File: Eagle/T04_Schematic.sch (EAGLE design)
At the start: 19 parts

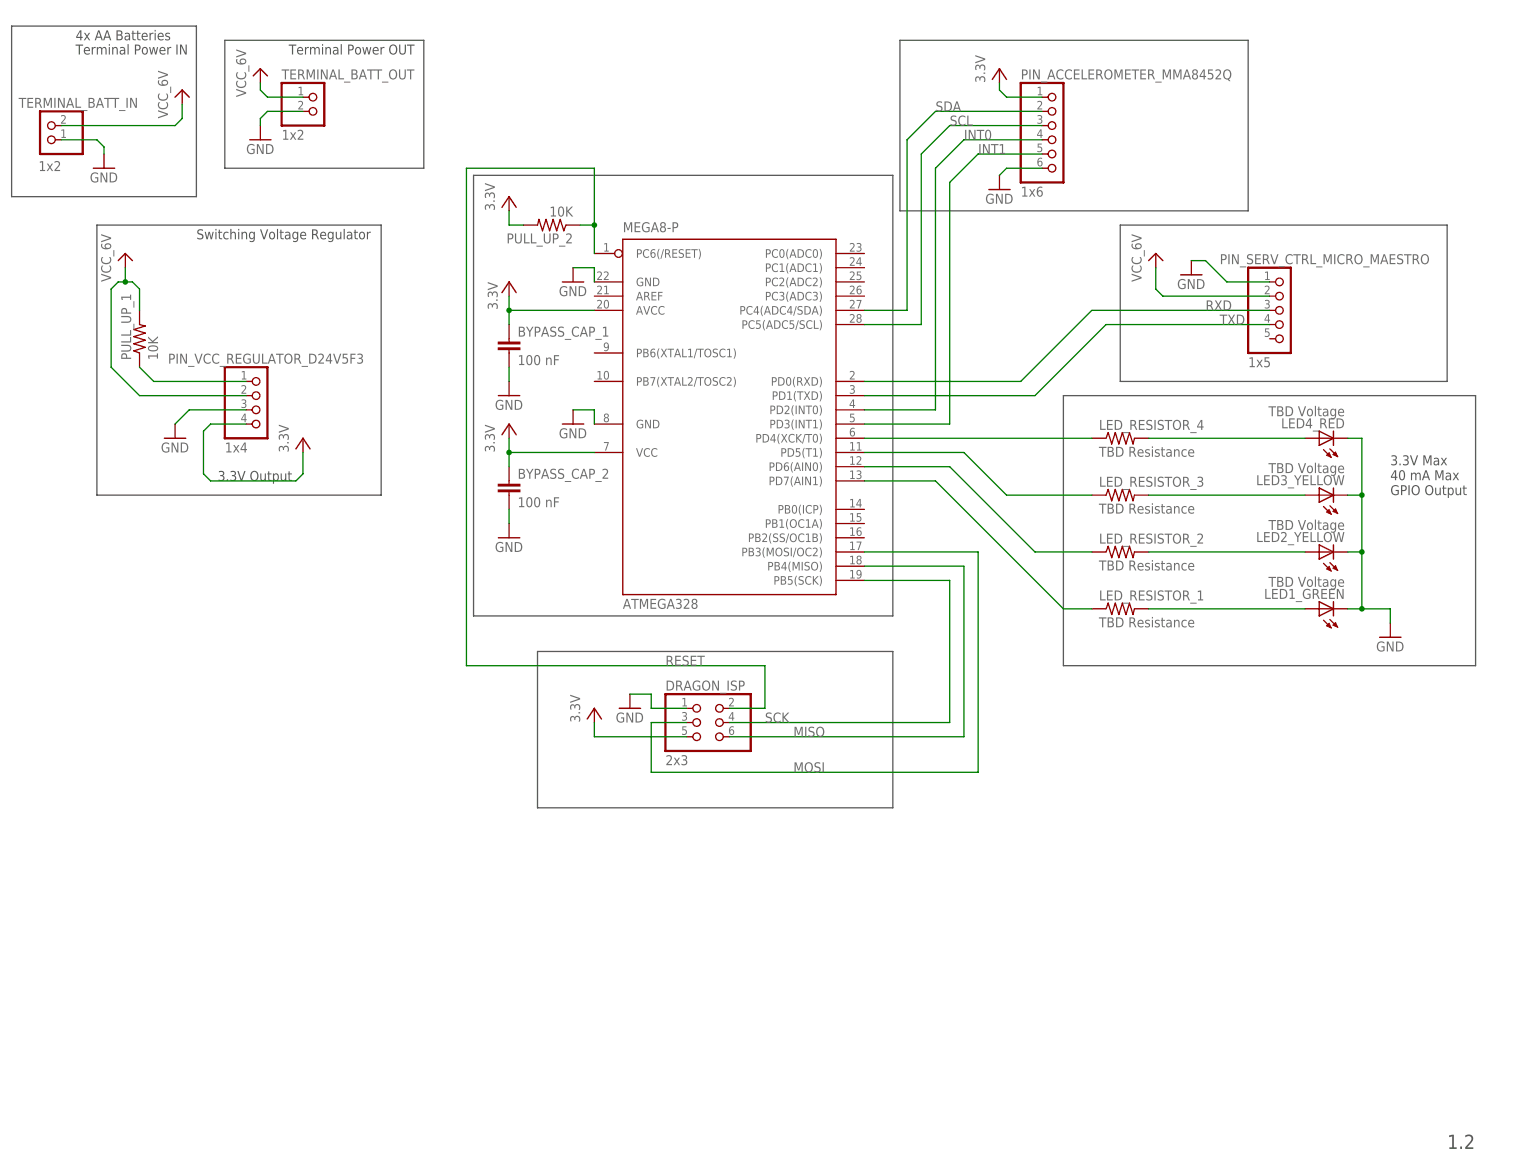
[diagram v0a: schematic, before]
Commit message: Schematic Updates
Updated with better supply layout and more organization.
Also changed filename to have team name.
Still Need: Oscillator, LEDs, UART review
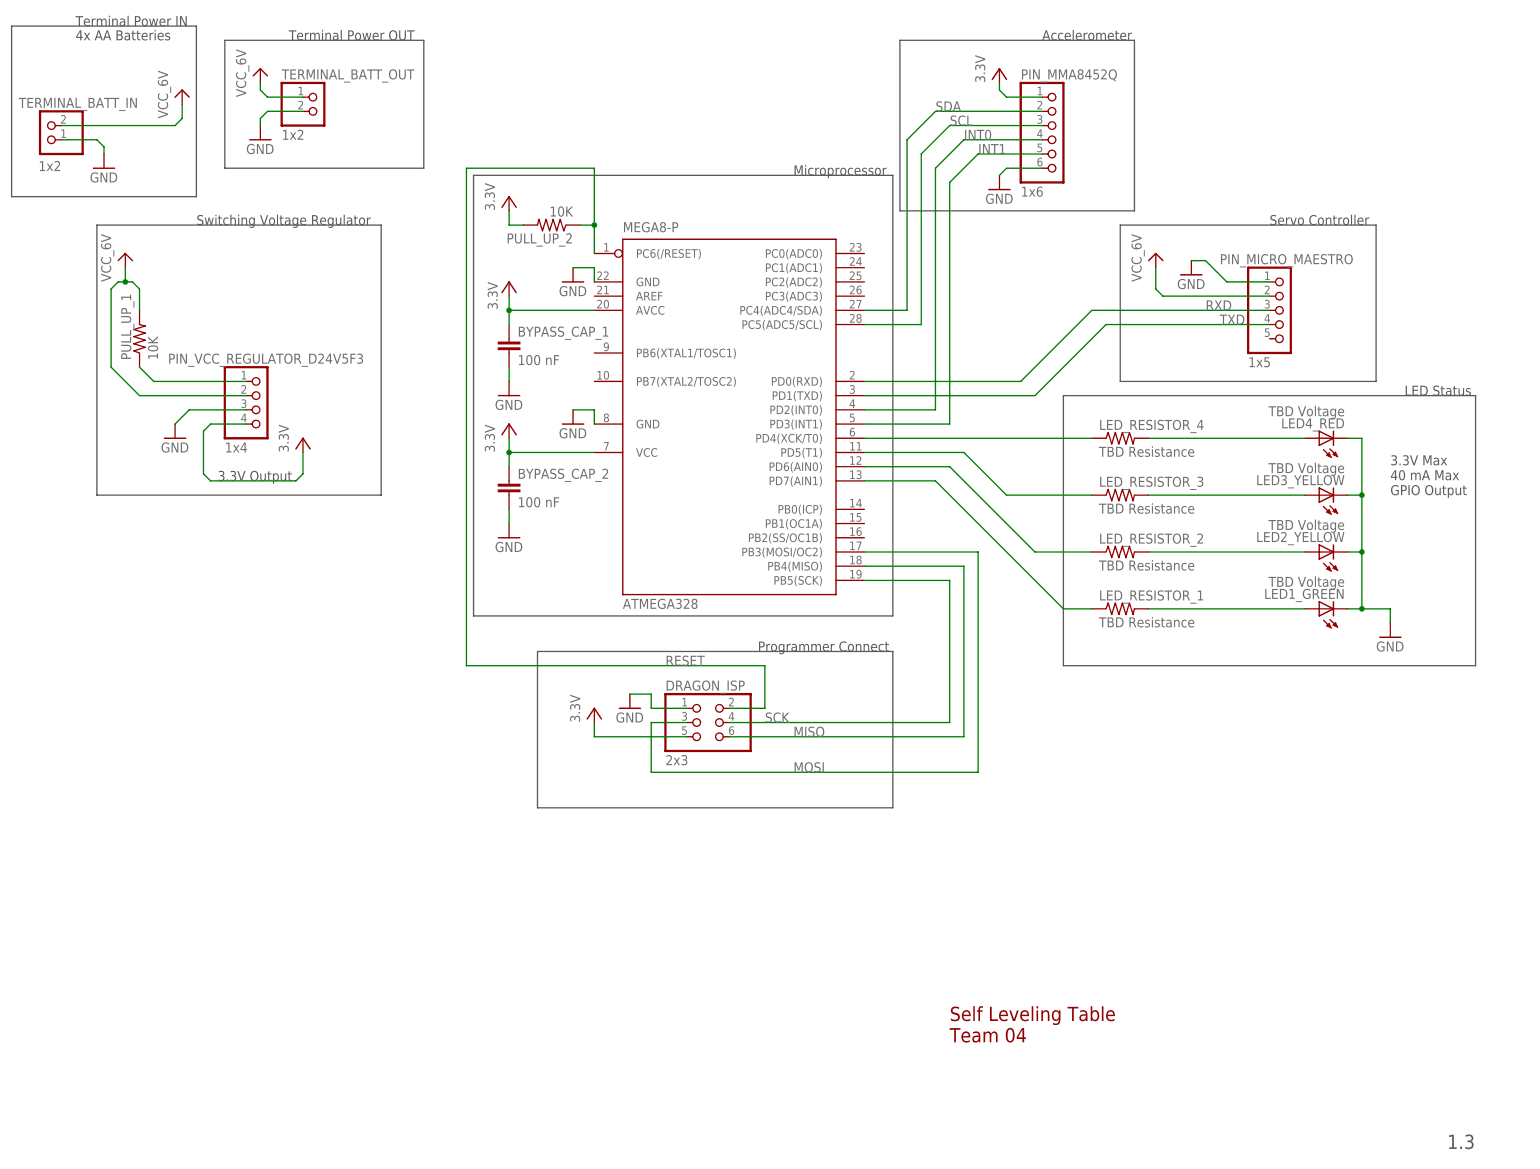
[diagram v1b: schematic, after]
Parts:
- renumbered PIN_ACCELEROMETER_MMA8452Q to PIN_MMA8452Q, PIN_SERV_CTRL_MICRO_MAESTRO to PIN_MICRO_MAESTRO
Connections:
- net VCC_3.3V renamed VCC
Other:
- note added: "1.3"
- note added: "Accelerometer"
- note added: "LED Status"
- note added: "Microprocessor"
- note added: "Programmer Connect"
- note added: "Self Leveling Table Team 04"
- note added: "Servo Controller"
- note removed: "1.2"
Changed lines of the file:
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@@
 <part name="FRAME1" library="frames" deviceset="FRAME_A_L" device=""/>
 <part name="ATMEGA328" library="atmel" deviceset="MEGA8-P" device=""/>
-<part name="PIN_ACCELEROMETER_MMA8452Q" library="pinhead" deviceset="PINHD-1X6" device="" value="1x6"/>
-<part name="PIN_SERV_CTRL_MICRO_MAESTRO" library="pinhead" deviceset="PINHD-1X5" device="" value="1x5"/>
+<part name="PIN_MMA8452Q" library="pinhead" deviceset="PINHD-1X6" device="" value="1x6"/>
+<part name="PIN_MICRO_MAESTRO" library="pinhead" deviceset="PINHD-1X5" device="" value="1x5"/>
 <part name="PIN_VCC_REGULATOR_D24V5F3" library="pinhead" deviceset="PINHD-1X4" device="" value="1x4"/>
 <part name="TERMINAL_BATT_IN" library="pinhead" deviceset="PINHD-1X2" device="" value="1x2"/>
@@
 <plain>
 <text x="6.35" y="154.94" size="1.778" layer="97">4x AA Batteries</text>
-<text x="251.46" y="-43.18" size="2.54" layer="97">1.2</text>
+<text x="251.46" y="-43.18" size="2.54" layer="97">1.3</text>
 <text x="241.3" y="73.66" size="1.778" layer="97">3.3V Max
 40 mA Max
@@
 <wire x1="256.54" y1="43.18" x2="182.88" y2="43.18" width="0.1524" layer="97"/>
 <wire x1="182.88" y1="43.18" x2="182.88" y2="91.44" width="0.1524" layer="97"/>
-<wire x1="153.67" y1="154.94" x2="215.9" y2="154.94" width="0.1524" layer="97"/>
-<wire x1="215.9" y1="154.94" x2="215.9" y2="124.46" width="0.1524" layer="97"/>
-<wire x1="215.9" y1="124.46" x2="153.67" y2="124.46" width="0.1524" layer="97"/>
+<wire x1="153.67" y1="154.94" x2="195.58" y2="154.94" width="0.1524" layer="97"/>
+<wire x1="195.58" y1="154.94" x2="195.58" y2="124.46" width="0.1524" layer="97"/>
+<wire x1="195.58" y1="124.46" x2="153.67" y2="124.46" width="0.1524" layer="97"/>
 <wire x1="153.67" y1="124.46" x2="153.67" y2="154.94" width="0.1524" layer="97"/>
-<wire x1="193.04" y1="121.92" x2="251.46" y2="121.92" width="0.1524" layer="97"/>
-<wire x1="251.46" y1="121.92" x2="251.46" y2="93.98" width="0.1524" layer="97"/>
-<wire x1="251.46" y1="93.98" x2="193.04" y2="93.98" width="0.1524" layer="97"/>
+<wire x1="193.04" y1="121.92" x2="238.76" y2="121.92" width="0.1524" layer="97"/>
+<wire x1="238.76" y1="121.92" x2="238.76" y2="93.98" width="0.1524" layer="97"/>
+<wire x1="238.76" y1="93.98" x2="193.04" y2="93.98" width="0.1524" layer="97"/>
 <wire x1="193.04" y1="93.98" x2="193.04" y2="121.92" width="0.1524" layer="97"/>
 <wire x1="88.9" y1="45.72" x2="152.4" y2="45.72" width="0.1524" layer="97"/>
@@
 <wire x1="152.4" y1="52.07" x2="77.47" y2="52.07" width="0.1524" layer="97"/>
 <wire x1="77.47" y1="52.07" x2="77.47" y2="130.81" width="0.1524" layer="97"/>
-<text x="6.35" y="152.4" size="1.778" layer="97">Terminal Power IN</text>
-<text x="44.45" y="152.4" size="1.778" layer="97">Terminal Power OUT</text>
-<text x="27.94" y="119.38" size="1.778" layer="97">Switching Voltage Regulator</text>
+<text x="6.35" y="157.48" size="1.778" layer="97">Terminal Power IN</text>
+<text x="44.45" y="154.94" size="1.778" layer="97">Terminal Power OUT</text>
+<text x="27.94" y="121.92" size="1.778" layer="97">Switching Voltage Regulator</text>
+<text x="162.56" y="-24.13" size="2.54" layer="94">Self Leveling Table
+Team 04</text>
+<text x="179.07" y="154.94" size="1.778" layer="97">Accelerometer</text>
+<text x="219.71" y="121.92" size="1.778" layer="97">Servo Controller</text>
+<text x="243.84" y="91.44" size="1.778" layer="97">LED Status</text>
+<text x="128.27" y="45.72" size="1.778" layer="97">Programmer Connect</text>
+<text x="134.62" y="130.81" size="1.778" layer="97">Microprocessor</text>
 </plain>
 <instances>
@@
 <instance part="FRAME1" gate="G$2" x="158.75" y="-50.8"/>
 <instance part="ATMEGA328" gate="G$1" x="121.92" y="88.9"/>
-<instance part="PIN_ACCELEROMETER_MMA8452Q" gate="A" x="181.61" y="137.16"/>
-<instance part="PIN_SERV_CTRL_MICRO_MAESTRO" gate="A" x="222.25" y="106.68" smashed="yes">
+<instance part="PIN_MMA8452Q" gate="A" x="181.61" y="137.16"/>
+<instance part="PIN_MICRO_MAESTRO" gate="A" x="222.25" y="106.68" smashed="yes">
 <attribute name="NAME" x="210.82" y="114.935" size="1.778" layer="95"/>
 <attribute name="VALUE" x="215.9" y="96.52" size="1.778" layer="96"/>
@@
 </segment>
 <segment>
-<pinref part="PIN_ACCELEROMETER_MMA8452Q" gate="A" pin="6"/>
+<pinref part="PIN_MMA8452Q" gate="A" pin="6"/>
 <pinref part="GND3" gate="1" pin="GND"/>
 <wire x1="171.45" y1="130.81" x2="172.72" y2="132.08" width="0.1524" layer="91"/>
@@
 <pinref part="GND4" gate="1" pin="GND"/>
 <wire x1="205.74" y1="115.57" x2="208.28" y2="115.57" width="0.1524" layer="91"/>
-<pinref part="PIN_SERV_CTRL_MICRO_MAESTRO" gate="A" pin="1"/>
+<pinref part="PIN_MICRO_MAESTRO" gate="A" pin="1"/>
 <wire x1="208.28" y1="115.57" x2="212.09" y2="111.76" width="0.1524" layer="91"/>
 <wire x1="212.09" y1="111.76" x2="219.71" y2="111.76" width="0.1524" layer="91"/>
@@
 <net name="SDA" class="0">
 <segment>
-<pinref part="PIN_ACCELEROMETER_MMA8452Q" gate="A" pin="2"/>
+<pinref part="PIN_MMA8452Q" gate="A" pin="2"/>
 <wire x1="179.07" y1="142.24" x2="160.02" y2="142.24" width="0.1524" layer="91"/>
 <label x="160.02" y="142.24" size="1.778" layer="95"/>
@@
 <net name="SCL" class="0">
 <segment>
-<pinref part="PIN_ACCELEROMETER_MMA8452Q" gate="A" pin="3"/>
+<pinref part="PIN_MMA8452Q" gate="A" pin="3"/>
 <wire x1="179.07" y1="139.7" x2="162.56" y2="139.7" width="0.1524" layer="91"/>
 <label x="162.56" y="139.7" size="1.778" layer="95"/>
@@
 <net name="INT0" class="0">
 <segment>
-<pinref part="PIN_ACCELEROMETER_MMA8452Q" gate="A" pin="4"/>
+<pinref part="PIN_MMA8452Q" gate="A" pin="4"/>
 <wire x1="179.07" y1="137.16" x2="165.1" y2="137.16" width="0.1524" layer="91"/>
 <label x="165.1" y="137.16" size="1.778" layer="95"/>
@@
 <pinref part="ATMEGA328" gate="G$1" pin="PD3(INT1)"/>
 <wire x1="162.56" y1="86.36" x2="147.32" y2="86.36" width="0.1524" layer="91"/>
-<pinref part="PIN_ACCELEROMETER_MMA8452Q" gate="A" pin="5"/>
+<pinref part="PIN_MMA8452Q" gate="A" pin="5"/>
 <wire x1="179.07" y1="134.62" x2="167.64" y2="134.62" width="0.1524" layer="91"/>
 <label x="167.64" y="134.62" size="1.778" layer="95"/>
@@
 </segment>
 </net>
-<net name="VCC_3.3V" class="0">
+<net name="VCC" class="0">
 <segment>
 <pinref part="P+1" gate="VCC" pin="VCC"/>
@@
 </segment>
 <segment>
-<pinref part="PIN_ACCELEROMETER_MMA8452Q" gate="A" pin="1"/>
+<pinref part="PIN_MMA8452Q" gate="A" pin="1"/>
 <wire x1="172.72" y1="144.78" x2="179.07" y2="144.78" width="0.1524" layer="91"/>
 <pinref part="P+5" gate="VCC" pin="VCC"/>
@@
 <pinref part="ATMEGA328" gate="G$1" pin="PD0(RXD)"/>
 <wire x1="147.32" y1="93.98" x2="175.26" y2="93.98" width="0.1524" layer="91"/>
-<pinref part="PIN_SERV_CTRL_MICRO_MAESTRO" gate="A" pin="3"/>
+<pinref part="PIN_MICRO_MAESTRO" gate="A" pin="3"/>
 <wire x1="187.96" y1="106.68" x2="219.71" y2="106.68" width="0.1524" layer="91"/>
 <label x="208.28" y="106.68" size="1.778" layer="95"/>
@@
 <pinref part="ATMEGA328" gate="G$1" pin="PD1(TXD)"/>
 <wire x1="147.32" y1="91.44" x2="177.8" y2="91.44" width="0.1524" layer="91"/>
-<pinref part="PIN_SERV_CTRL_MICRO_MAESTRO" gate="A" pin="4"/>
+<pinref part="PIN_MICRO_MAESTRO" gate="A" pin="4"/>
 <wire x1="190.5" y1="104.14" x2="219.71" y2="104.14" width="0.1524" layer="91"/>
 <label x="210.82" y="104.14" size="1.778" layer="95"/>
@@
 </segment>
 <segment>
-<pinref part="PIN_SERV_CTRL_MICRO_MAESTRO" gate="A" pin="2"/>
+<pinref part="PIN_MICRO_MAESTRO" gate="A" pin="2"/>
 <wire x1="219.71" y1="109.22" x2="200.66" y2="109.22" width="0.1524" layer="91"/>
 <wire x1="200.66" y1="109.22" x2="199.39" y2="110.49" width="0.1524" layer="91"/>

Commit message: Small Schematic Update
Minor tweaks, notes
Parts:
- added C1, C2: 22pF, rcl:C-EUC1206
- added LED5_BLUE: TBD Voltage, led:LEDSMT1206
- added LED_DECORATION: 1x2, pinhead:PINHD-1X2
- added LED_RESISTOR_5: TBD Resistance, rcl:R-US_R1206
- added Y1: 16 MHz, SparkFun-FreqCtrl:CRYSTALHC49US
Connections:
- new net CLOCK: ATMEGA328.PB0(ICP), LED_DECORATION.1
- new net N$1: LED5_BLUE.A, LED_RESISTOR_5.2
- new net N$7: ATMEGA328.PB1(OC1A), LED_DECORATION.2
- new net XTAL1: ATMEGA328.PB6(XTAL1/TOSC1), C1.1, Y1.1
- new net XTAL2: ATMEGA328.PB7(XTAL2/TOSC2), C2.1, Y1.2
- net GND: now also C1.2, C2.2, LED5_BLUE.C
- net VCC_6V: now also LED_RESISTOR_5.1
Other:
- note added: "Board Power LED"
- note added: "DO THESE CROSS?"
- note added: "External Clock"
- note added: "Fix this stuuuuuuuf"
- moved on the sheet: BYPASS_CAP_2
